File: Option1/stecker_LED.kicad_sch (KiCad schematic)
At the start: 1 part, among them J701 Conn_01x02_Socket

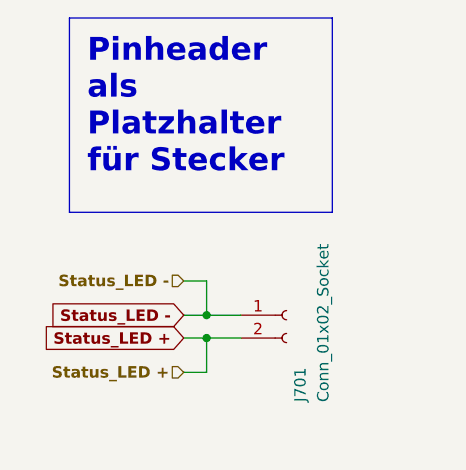
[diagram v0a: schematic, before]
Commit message: SPI Flash hinzugefügt, IN/Outputs vereinheitlicht, USB Flash Möglichkeit hinzugefügt, Display fehtl noch
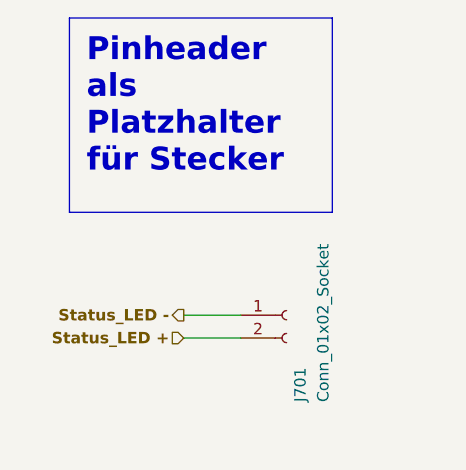
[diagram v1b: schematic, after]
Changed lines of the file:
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@@
 (kicad_sch
-	(version 20231120)
+	(version 20250114)
 	(generator "eeschema")
-	(generator_version "8.0")
+	(generator_version "9.0")
 	(paper "A4")
 	(title_block
@@
 		(comment 3 "Sebastian Hampl")
 	)
-	(junction
-		(at 35.56 55.88)
-		(diameter 0)
-		(color 0 0 0 0)
-	)
-	(junction
-		(at 35.56 53.34)
-		(diameter 0)
-		(color 0 0 0 0)
-	)
-	(wire
-		(pts
-			(xy 35.56 53.34) (xy 39.37 53.34)
-		)
-		(stroke
-			(width 0)
-			(type default)
-		)
-	)
-	(wire
-		(pts
-			(xy 33.02 59.69) (xy 35.56 59.69)
-		)
-		(stroke
-			(width 0)
-			(type default)
-		)
-	)
-	(wire
-		(pts
-			(xy 35.56 59.69) (xy 35.56 55.88)
-		)
-		(stroke
-			(width 0)
-			(type default)
-		)
-	)
-	(wire
-		(pts
-			(xy 33.02 49.53) (xy 35.56 49.53)
-		)
-		(stroke
-			(width 0)
-			(type default)
-		)
-	)
-	(wire
-		(pts
-			(xy 35.56 55.88) (xy 39.37 55.88)
-		)
-		(stroke
-			(width 0)
-			(type default)
-		)
-	)
-	(wire
-		(pts
-			(xy 33.02 55.88) (xy 35.56 55.88)
-		)
-		(stroke
-			(width 0)
-			(type default)
-		)
-	)
-	(wire
-		(pts
-			(xy 33.02 53.34) (xy 35.56 53.34)
-		)
-		(stroke
-			(width 0)
-			(type default)
-		)
-	)
-	(wire
-		(pts
-			(xy 35.56 49.53) (xy 35.56 53.34)
-		)
-		(stroke
-			(width 0)
-			(type default)
-		)
-	)
 	(text_box "Pinheader als Platzhalter für Stecker"
 		(exclude_from_sim no)
 		(at 20.32 20.32 0)
 		(size 29.21 21.59)
+		(margins 1.905 1.905 1.905 1.905)
 		(stroke
 			(width 0)
@@
 		)
 	)
-	(global_label "Status_LED -"
-		(shape input)
-		(at 33.02 53.34 180)
-		(fields_autoplaced yes)
-		(effects
-			(font
-				(size 1.27 1.27)
-				(thickness 0.254)
-				(bold yes)
-			)
-			(justify right)
+	(wire
+		(pts
+			(xy 33.02 55.88) (xy 39.37 55.88)
 		)
-		(property "Intersheetrefs" "${INTERSHEET_REFS}"
-			(at 16.6171 53.34 0)
-			(effects
-				(font
-					(size 1.27 1.27)
-				)
-				(justify right)
-				(hide yes)
-			)
+		(stroke
+			(width 0)
+			(type default)
 		)
 	)
-	(global_label "Status_LED +"
-		(shape input)
-		(at 33.02 55.88 180)
-		(fields_autoplaced yes)
-		(effects
-			(font
-				(size 1.27 1.27)
-				(thickness 0.254)
-				(bold yes)
-			)
-			(justify right)
+	(wire
+		(pts
+			(xy 33.02 53.34) (xy 39.37 53.34)
 		)
-		(property "Intersheetrefs" "${INTERSHEET_REFS}"
-			(at 16.6171 55.88 0)
-			(effects
-				(font
-					(size 1.27 1.27)
-				)
-				(justify right)
-				(hide yes)
-			)
+		(stroke
+			(width 0)
+			(type default)
 		)
 	)
 	(hierarchical_label "Status_LED +"
 		(shape input)
-		(at 33.02 59.69 180)
+		(at 33.02 55.88 180)
 		(effects
 			(font
@@
 	)
 	(hierarchical_label "Status_LED -"
-		(shape input)
-		(at 33.02 49.53 180)
+		(shape output)
+		(at 33.02 53.34 180)
 		(effects
 			(font

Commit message: Layout komplett bis auf RFID Leiste und 3V3 Erzeugung Display
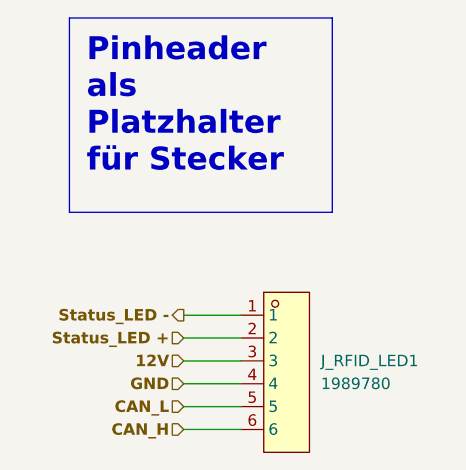
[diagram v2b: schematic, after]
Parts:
- removed J701: Conn_01x02_Socket, Connector_PinHeader_2.54mm:PinHeader_1x02_P2.54mm_Vertical, symbol Connector:Conn_01x02_Socket
- added J_RFID_LED1: 1989780, easyeda2kicad:CONN-TH_6P-P2.50_1989780, symbol EasyEda2KiCad:1989780
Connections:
- net Status_LED +: now also J_RFID_LED1.2
- net Status_LED -: now also J_RFID_LED1.1
- new net 12V: J_RFID_LED1.3
- new net CAN_H: J_RFID_LED1.6
- new net CAN_L: J_RFID_LED1.5
- new net GND: J_RFID_LED1.4
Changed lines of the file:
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@@
+	(wire
+		(pts
+			(xy 33.02 63.5) (xy 39.37 63.5)
+		)
+		(stroke
+			(width 0)
+			(type default)
+		)
+	)
+	(wire
+		(pts
+			(xy 33.02 58.42) (xy 39.37 58.42)
+		)
+		(stroke
+			(width 0)
+			(type default)
+		)
+	)
 	(wire
 		(pts
@@
 		)
 	)
+	(wire
+		(pts
+			(xy 33.02 66.04) (xy 39.37 66.04)
+		)
+		(stroke
+			(width 0)
+			(type default)
+		)
+	)
+	(wire
+		(pts
+			(xy 33.02 60.96) (xy 39.37 60.96)
+		)
+		(stroke
+			(width 0)
+			(type default)
+		)
+	)
+	(hierarchical_label "CAN_L"
+		(shape input)
+		(at 33.02 63.5 180)
+		(effects
+			(font
+				(size 1.27 1.27)
+				(thickness 0.254)
+				(bold yes)
+			)
+			(justify right)
+		)
+	)
 	(hierarchical_label "Status_LED +"
 		(shape input)
 		(at 33.02 55.88 180)
+		(effects
+			(font
+				(size 1.27 1.27)
+				(thickness 0.254)
+				(bold yes)
+			)
+			(justify right)
+		)
+	)
+	(hierarchical_label "CAN_H"
+		(shape input)
+		(at 33.02 66.04 180)
+		(effects
+			(font
+				(size 1.27 1.27)
+				(thickness 0.254)
+				(bold yes)
+			)
+			(justify right)
+		)
+	)
+	(hierarchical_label "GND"
+		(shape input)
+		(at 33.02 60.96 180)
 		(effects
 			(font
@@
 		)
 	)
+	(hierarchical_label "12V"
+		(shape input)
+		(at 33.02 58.42 180)
+		(effects
+			(font
+				(size 1.27 1.27)
+				(thickness 0.254)
+				(bold yes)
+			)
+			(justify right)
+		)
+	)
 	(symbol
-		(lib_id "Connector:Conn_01x02_Socket")
-		(at 44.45 53.34 0)
+		(lib_id "EasyEda2KiCad:1989780")
+		(at 44.45 59.69 0)
 		(unit 1)
 		(exclude_from_sim no)
@@
 		(on_board yes)
 		(dnp no)
-		(property "Reference" "J701"
-			(at 45.974 62.992 90)
+		(fields_autoplaced yes)
+		(property "Reference" "J_RFID_LED1"
+			(at 48.26 58.4199 0)
 			(effects
 				(font
@@
 			)
 		)
-		(property "Value" "Conn_01x02_Socket"
-			(at 48.514 62.992 90)
+		(property "Value" "1989780"
+			(at 48.26 60.9599 0)
 			(effects
 				(font
@@
 			)
 		)
-		(property "Footprint" "Connector_PinHeader_2.54mm:PinHeader_1x02_P2.54mm_Vertical"
-			(at 44.45 53.34 0)
+		(property "Footprint" "easyeda2kicad:CONN-TH_6P-P2.50_1989780"
+			(at 44.45 73.66 0)
 			(effects
 				(font
@@
 			)
 		)
-		(property "Datasheet" "~"
-			(at 44.45 53.34 0)
+		(property "Datasheet" ""
+			(at 44.45 59.69 0)
 			(effects
 				(font
@@
 			)
 		)
-		(property "Description" "Generic connector, single row, 01x02, script generated"
-			(at 44.45 53.34 0)
+		(property "Description" ""
+			(at 44.45 59.69 0)
 			(effects
 				(font
@@
 			)
 		)
+		(property "LCSC Part" "C5443580"
+			(at 44.45 76.2 0)
+			(effects
+				(font
+					(size 1.27 1.27)
+				)
+				(hide yes)
+			)
+		)
+		(pin "6"
+		)
 		(pin "2"
+		)
+		(pin "4"
+		)
+		(pin "3"
+		)
+		(pin "5"
 		)
 		(pin "1"
 		)
 		(instances
-			(project ""
+			(project "Option1"
 				(path "/b9e5f262-9648-4b79-bdd1-af888b822329/85d62a2c-6dc6-478e-aff1-38efc7ff1a87"
-					(reference "J701")
+					(reference "J_RFID_LED1")
 					(unit 1)
 				)

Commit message: Platine korrigeiert, 5V DCDC getauscht, 3.3V Display Versorgung entfernt. Bauteile neu angeordnet, USB 5V auf 5V Supply geführt
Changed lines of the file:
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@@
 		(comment 3 "Sebastian Hampl")
-	)
-	(text_box "Pinheader als Platzhalter für Stecker"
-		(exclude_from_sim no)
-		(at 20.32 20.32 0)
-		(size 29.21 21.59)
-		(margins 1.905 1.905 1.905 1.905)
-		(stroke
-			(width 0)
-			(type default)
-		)
-		(fill
-			(type none)
-		)
-		(effects
-			(font
-				(size 2.54 2.54)
-				(thickness 0.254)
-				(bold yes)
-				(color 245 0 0 1)
-			)
-			(justify left top)
-		)
 	)
 	(wire

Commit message: power Supply angepasst für 12V und 48V, Datenblätter für DCDCs hinzugefügt
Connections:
- net CAN_H is gone; now on net GND: J_RFID_LED1.6
- net GND: no longer J_RFID_LED1.4
- net CAN_L renamed 3.3V
- new net 5V: J_RFID_LED1.4
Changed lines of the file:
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@@
+	(wire
+		(pts
+			(xy 33.02 60.96) (xy 39.37 60.96)
+		)
+		(stroke
+			(width 0)
+			(type default)
+		)
+	)
 	(wire
 		(pts
@@
 		)
 	)
-	(wire
-		(pts
-			(xy 33.02 60.96) (xy 39.37 60.96)
-		)
-		(stroke
-			(width 0)
-			(type default)
-		)
-	)
-	(hierarchical_label "CAN_L"
+	(hierarchical_label "5V"
 		(shape input)
-		(at 33.02 63.5 180)
+		(at 33.02 60.96 180)
 		(effects
 			(font
@@
 		)
 	)
-	(hierarchical_label "CAN_H"
+	(hierarchical_label "GND"
 		(shape input)
 		(at 33.02 66.04 180)
-		(effects
-			(font
-				(size 1.27 1.27)
-				(thickness 0.254)
-				(bold yes)
-			)
-			(justify right)
-		)
-	)
-	(hierarchical_label "GND"
-		(shape input)
-		(at 33.02 60.96 180)
 		(effects
 			(font
@@
 		(effects
 			(font
+				(size 1.27 1.27)
+				(thickness 0.254)
+				(bold yes)
+			)
+			(justify right)
+		)
+	)
+	(hierarchical_label "3.3V"
+		(shape input)
+		(at 33.02 63.5 180)
+		(effects
+			(font
